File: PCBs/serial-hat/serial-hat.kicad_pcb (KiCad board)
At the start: 2 copper layers, 65 x 56 mm, 15 parts, among them CN1 Modem port, CN2 Printer port, J1 Conn_01x02_Pin, J7 Rpi headers, U1 PC817C-S, U2 MAX3232

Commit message: Update stls and notes
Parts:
- added SW7: SW_SPST, Colins-Kicad:SPST momentary switch C6575016, F.Cu at (127.8, 96.0)
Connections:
- J7 pad 5: unconnected-(J7-Pin_5-Pad5) -> PWR_BTN
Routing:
- net PWR_BTN: track 0.00 -> 46.1 mm
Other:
- outline, holes or cut-outs redrawn

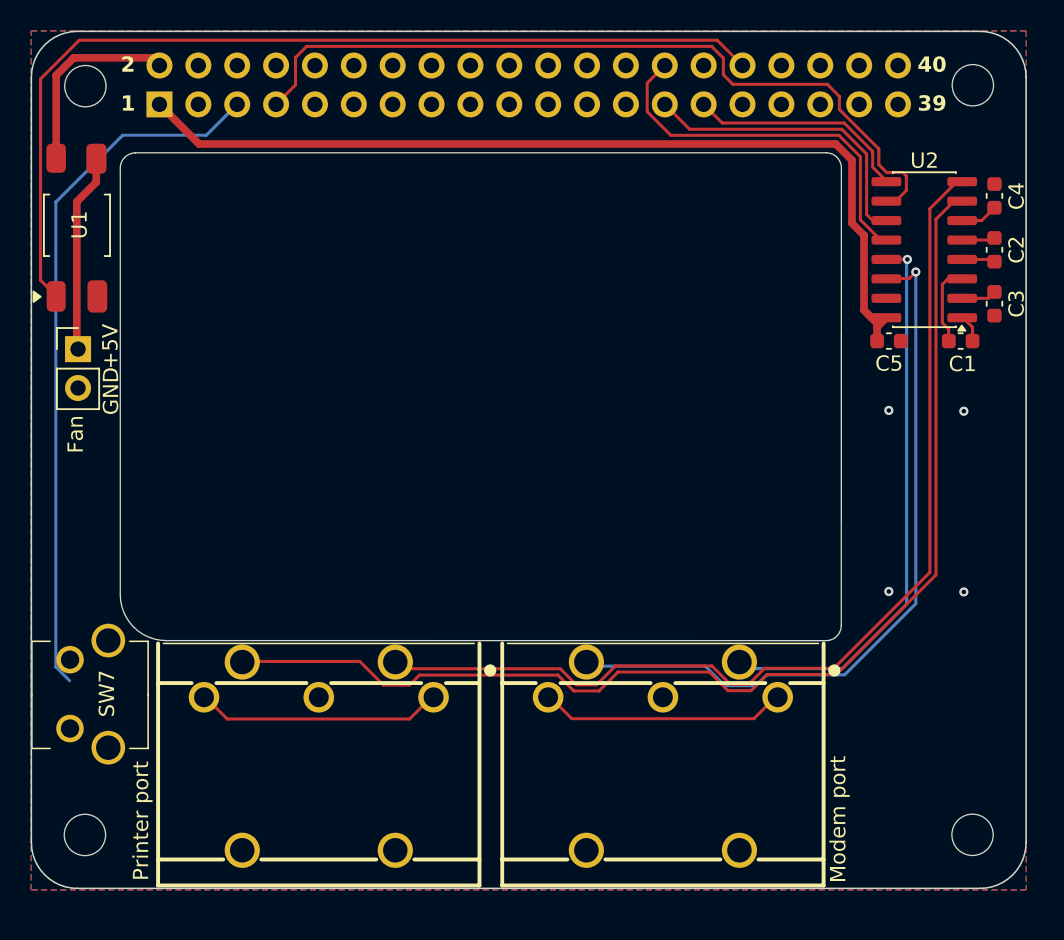
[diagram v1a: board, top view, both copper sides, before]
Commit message: Add teardrops
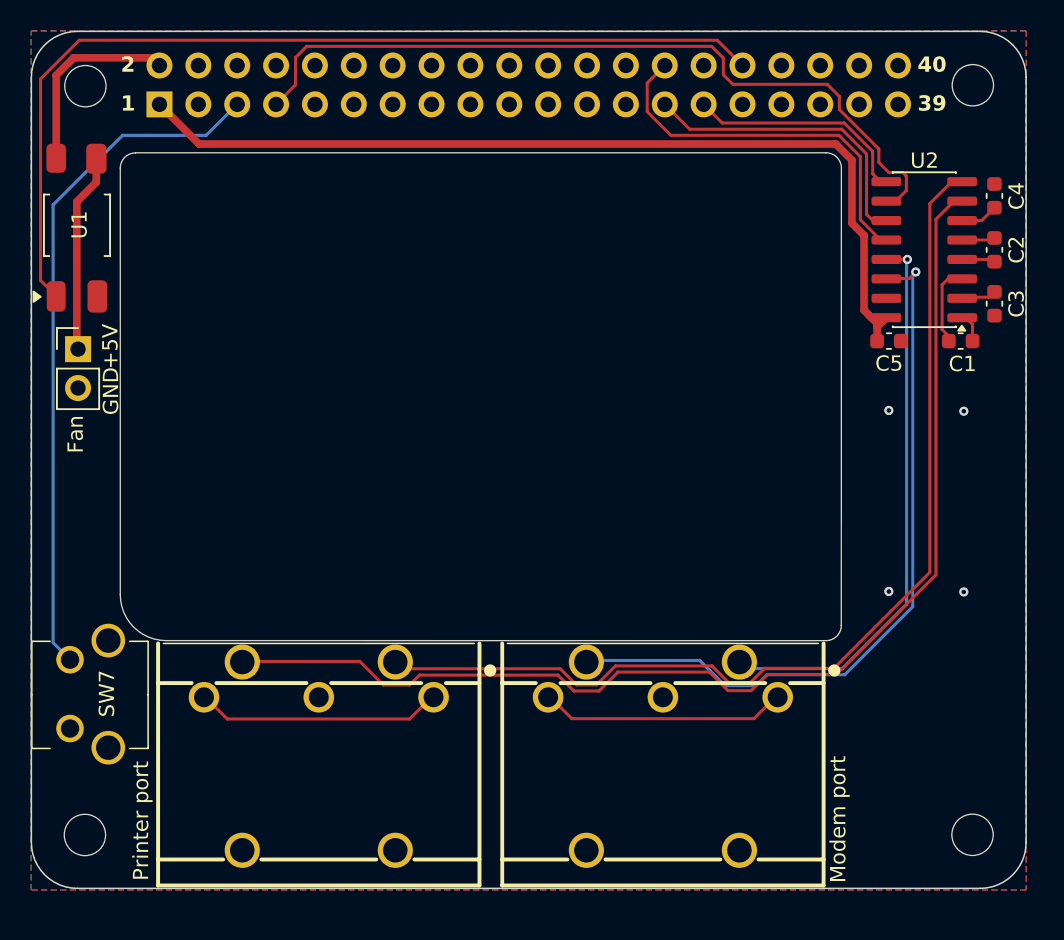
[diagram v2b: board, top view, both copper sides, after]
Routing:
- net PWR_BTN: track 46.1 -> 44.9 mm
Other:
- board text added: "Apple II serial hat for Pi 4/5 Colin Leroy-Mira, https://colino.net"
- board text removed: "Apple II serial hat for Pi 4/5"
- board text removed: "colino.net"

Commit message: Add fan mounting holes
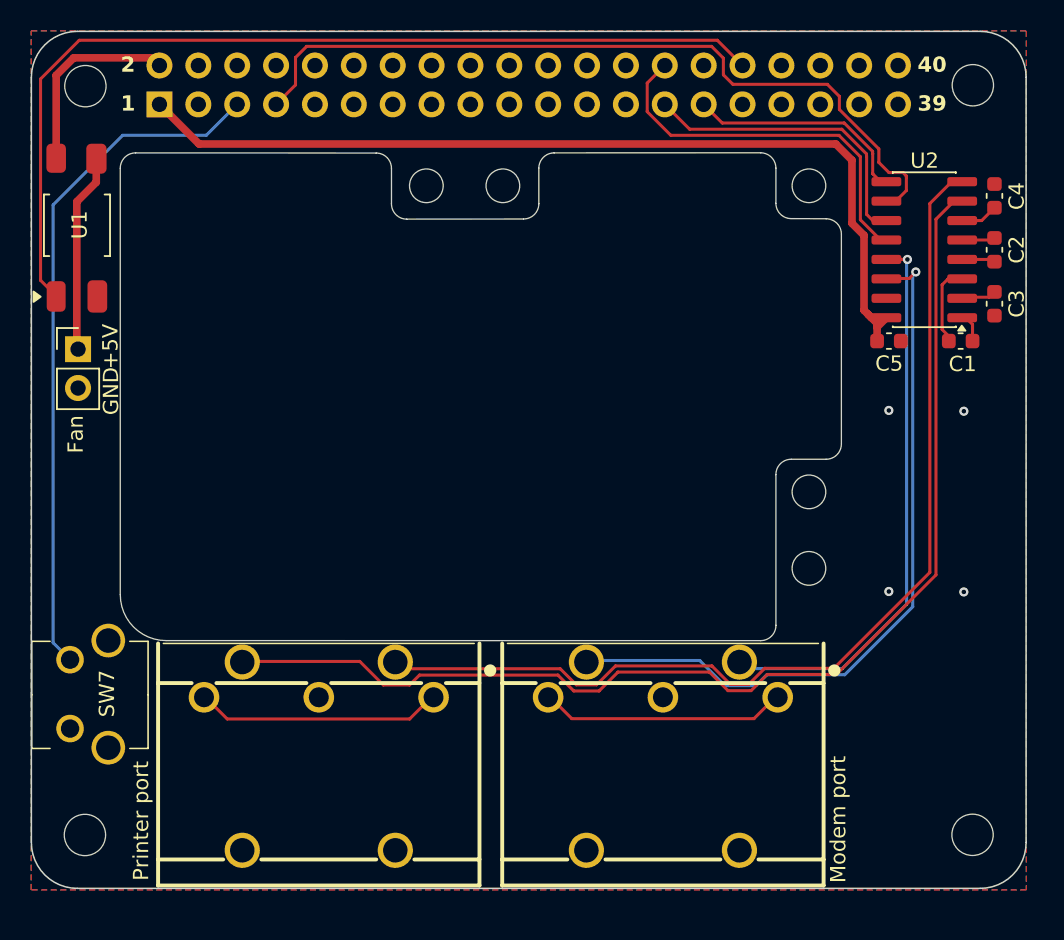
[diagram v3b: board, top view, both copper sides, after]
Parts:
- added REF**: MountingHole_2.2mm_M2_DIN965, MountingHole:MountingHole_2.2mm_M2_DIN965, F.Cu at (148.5, 62.7)
- added REF**: MountingHole_2.2mm_M2_DIN965, MountingHole:MountingHole_2.2mm_M2_DIN965, F.Cu at (153.5, 62.7)
- added REF**: MountingHole_2.2mm_M2_DIN965, MountingHole:MountingHole_2.2mm_M2_DIN965, F.Cu at (173.5, 82.7)
- added REF**: MountingHole_2.2mm_M2_DIN965, MountingHole:MountingHole_2.2mm_M2_DIN965, F.Cu at (173.5, 62.7)
- added REF**: MountingHole_2.2mm_M2_DIN965, MountingHole:MountingHole_2.2mm_M2_DIN965, F.Cu at (173.5, 87.7)
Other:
- outline, holes or cut-outs redrawn
